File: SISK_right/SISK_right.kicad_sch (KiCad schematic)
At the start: 86 parts, among them J1 OLED_128x32, J2 Battery Conn, SW1 "6", SW10 "Z", SW11 "U", SW12 "I", SW13 "O", SW14 "P", SW15 "Ü", SW16 "*", SW17 "Enter", SW18 "Del", SW19 "H", SW2 "7", SW20 "J", SW21 "K", SW22 "L", SW23 "Ö", SW24 "Ä", SW25 "'", SW26 "PGUP", SW27 "N", SW28 "M", SW29 ";", SW3 "8", SW30 ":", SW31 "-", SW32 "shift_R", SW33 "UP", SW34 "PGDOWN", SW35 "SPACE_R", SW36 "Alt", SW37 FN, SW38 "Ctrl", SW39 "Left", SW4 "9", SW40 "Down", SW41 "Right", SW5 "0", SW6 "ß", SW7 "`", SW8 "Backspace", SW9 "^", U1 Nice_Nano_V2

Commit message: changed nice nano footprint
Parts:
- U1: footprint ScottoKeebs_MCU:Arduino_Pro_Micro -> nice-nano-kicad-master:nice_nano
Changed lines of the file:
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@@
 			)
 		)
-		(property "Footprint" "ScottoKeebs_MCU:Arduino_Pro_Micro"
+		(property "Footprint" "nice-nano-kicad-master:nice_nano"
 			(at 232.41 96.52 0)
 			(effects

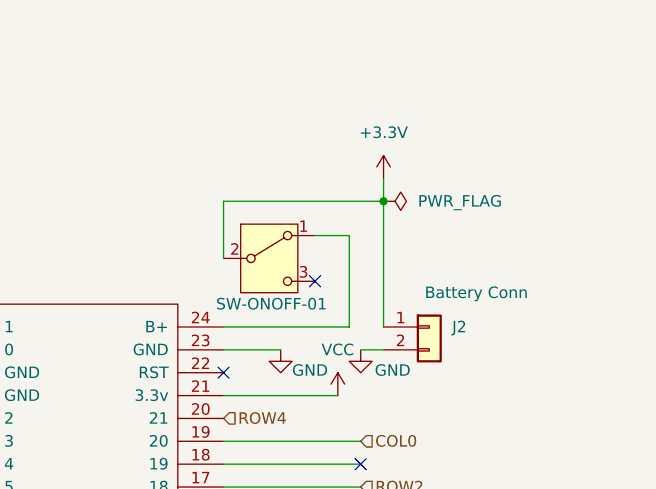
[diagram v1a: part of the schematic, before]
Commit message: added some text and alternative header for Power Switch
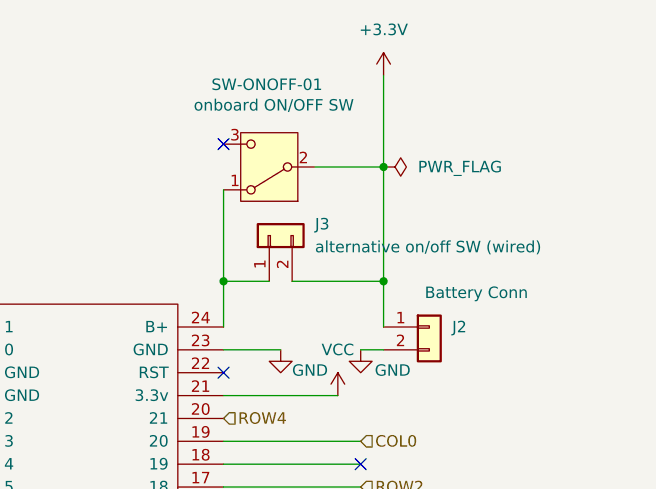
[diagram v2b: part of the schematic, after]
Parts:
- added J3: alternative on/off SW (wired), Connector_PinHeader_2.54mm:PinHeader_1x02_P2.54mm_Vertical, symbol Connector_Generic:Conn_01x02
- SW-ONOFF-01: value ~ -> onboard ON/OFF SW
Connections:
- net +3.3V: now also J3.2 (Pin_2)
- net at SW-ONOFF-01.1 (A), U1.24 (B+): now also J3.1 (Pin_1)
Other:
- moved on the sheet: SW-ONOFF-01
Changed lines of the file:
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@@
 	)
 	(junction
+		(at 265.43 41.91)
+		(diameter 0)
+		(color 0 0 0 0)
+	)
+	(junction
 		(at 74.93 85.09)
 		(diameter 0)
@@
 	)
 	(junction
+		(at 247.65 54.61)
+		(diameter 0)
+		(color 0 0 0 0)
+	)
+	(junction
 		(at 147.32 60.96)
 		(diameter 0)
@@
 	)
 	(junction
-		(at 265.43 45.72)
-		(diameter 0)
-		(color 0 0 0 0)
-	)
-	(junction
 		(at 116.84 60.96)
 		(diameter 0)
@@
 	)
 	(junction
+		(at 265.43 54.61)
+		(diameter 0)
+		(color 0 0 0 0)
+	)
+	(junction
 		(at 180.34 46.99)
 		(diameter 0)
@@
 	)
 	(no_connect
-		(at 257.81 54.61)
+		(at 247.65 39.37)
 	)
 	(no_connect
@@
 	(wire
 		(pts
-			(xy 261.62 49.53) (xy 257.81 49.53)
+			(xy 247.65 59.69) (xy 247.65 54.61)
 		)
 		(stroke
@@
 	(wire
 		(pts
-			(xy 247.65 52.07) (xy 247.65 45.72)
+			(xy 127 90.17) (xy 127 92.71)
 		)
 		(stroke
@@
 	(wire
 		(pts
-			(xy 127 90.17) (xy 127 92.71)
+			(xy 111.76 113.03) (xy 127 113.03)
 		)
 		(stroke
@@
 	(wire
 		(pts
-			(xy 111.76 113.03) (xy 127 113.03)
+			(xy 265.43 54.61) (xy 265.43 59.69)
 		)
 		(stroke
@@
 	(wire
 		(pts
-			(xy 261.62 59.69) (xy 261.62 49.53)
-		)
-		(stroke
-			(width 0)
-			(type default)
-		)
-	)
-	(wire
-		(pts
 			(xy 173.99 57.15) (xy 190.5 57.15)
 		)
@@
 	(wire
 		(pts
-			(xy 265.43 43.18) (xy 265.43 45.72)
-		)
-		(stroke
-			(width 0)
-			(type default)
-		)
-	)
-	(wire
-		(pts
 			(xy 217.17 67.31) (xy 210.82 67.31)
 		)
@@
 	(wire
 		(pts
-			(xy 247.65 59.69) (xy 261.62 59.69)
+			(xy 255.27 54.61) (xy 265.43 54.61)
+		)
+		(stroke
+			(width 0)
+			(type default)
+		)
+	)
+	(wire
+		(pts
+			(xy 247.65 54.61) (xy 247.65 44.45)
 		)
 		(stroke
@@
 	(wire
 		(pts
+			(xy 265.43 41.91) (xy 257.81 41.91)
+		)
+		(stroke
+			(width 0)
+			(type default)
+		)
+	)
+	(wire
+		(pts
 			(xy 127 85.09) (xy 142.24 85.09)
 		)
@@
 	(wire
 		(pts
+			(xy 265.43 31.75) (xy 265.43 41.91)
+		)
+		(stroke
+			(width 0)
+			(type default)
+		)
+	)
+	(wire
+		(pts
 			(xy 111.76 46.99) (xy 111.76 49.53)
 		)
@@
 	(wire
 		(pts
+			(xy 247.65 54.61) (xy 252.73 54.61)
+		)
+		(stroke
+			(width 0)
+			(type default)
+		)
+	)
+	(wire
+		(pts
 			(xy 83.82 90.17) (xy 83.82 104.14)
 		)
@@
 	(wire
 		(pts
-			(xy 265.43 45.72) (xy 265.43 59.69)
+			(xy 265.43 41.91) (xy 265.43 54.61)
 		)
 		(stroke
@@
 	(wire
 		(pts
-			(xy 247.65 45.72) (xy 265.43 45.72)
-		)
-		(stroke
-			(width 0)
-			(type default)
-		)
-	)
-	(wire
-		(pts
 			(xy 74.93 100.33) (xy 57.15 100.33)
 		)
@@
 	(symbol
 		(lib_id "power:PWR_FLAG")
-		(at 265.43 45.72 270)
+		(at 265.43 41.91 270)
 		(unit 1)
 		(exclude_from_sim no)
@@
 		(fields_autoplaced yes)
 		(property "Reference" "#FLG01"
-			(at 267.335 45.72 0)
+			(at 267.335 41.91 0)
 			(effects
 				(font
@@
 		)
 		(property "Value" "PWR_FLAG"
-			(at 269.24 45.7199 90)
+			(at 269.24 41.9099 90)
 			(effects
 				(font
@@
 		)
 		(property "Footprint" ""
-			(at 265.43 45.72 0)
+			(at 265.43 41.91 0)
 			(effects
 				(font
@@
 		)
 		(property "Datasheet" "~"
-			(at 265.43 45.72 0)
+			(at 265.43 41.91 0)
 			(effects
 				(font
@@
 		)
 		(property "Description" "Special symbol for telling ERC where power comes from"
-			(at 265.43 45.72 0)
+			(at 265.43 41.91 0)
 			(effects
 				(font
@@
 	)
 	(symbol
+		(lib_id "Connector_Generic:Conn_01x02")
+		(at 252.73 49.53 90)
+		(unit 1)
+		(exclude_from_sim no)
+		(in_bom yes)
+		(on_board yes)
+		(dnp no)
+		(fields_autoplaced yes)
+		(property "Reference" "J3"
+			(at 257.81 48.2599 90)
+			(effects
+				(font
+					(size 1.27 1.27)
+				)
+				(justify right)
+			)
+		)
+		(property "Value" "alternative on/off SW (wired)"
+			(at 257.81 50.7999 90)
+			(effects
+				(font
+					(size 1.27 1.27)
+				)
+				(justify right)
+			)
+		)
+		(property "Footprint" "Connector_PinHeader_2.54mm:PinHeader_1x02_P2.54mm_Vertical"
+			(at 252.73 49.53 0)
+			(effects
+				(font
+					(size 1.27 1.27)
+				)
+				(hide yes)
+			)
+		)
+		(property "Datasheet" "~"
+			(at 252.73 49.53 0)
+			(effects
+				(font
+					(size 1.27 1.27)
+				)
+				(hide yes)
+			)
+		)
+		(property "Description" "Generic connector, single row, 01x02, script generated (kicad-library-utils/schlib/autogen/connector/)"
+			(at 252.73 49.53 0)
+			(effects
+				(font
+					(size 1.27 1.27)
+				)
+				(hide yes)
+			)
+		)
+		(pin "2"
+		)
+		(pin "1"
+		)
+		(instances
+			(project ""
+				(path "/257e25c7-95c4-4199-9825-6959824a558c"
+					(reference "J3")
+					(unit 1)
+				)
+			)
+		)
+	)
+	(symbol
 		(lib_id "Device:D")
 		(at 173.99 52.07 90)
@@
 	(symbol
 		(lib_id "Switch:SW_SPDT")
-		(at 252.73 52.07 0)
+		(at 252.73 41.91 180)
 		(unit 1)
 		(exclude_from_sim no)
@@
 		(dnp no)
 		(property "Reference" "SW-ONOFF-01"
-			(at 252.984 57.15 0)
+			(at 252.476 32.766 0)
 			(effects
 				(font
@@
 			)
 		)
-		(property "Value" "~"
-			(at 252.73 46.99 0)
+		(property "Value" "onboard ON/OFF SW"
+			(at 253.238 35.052 0)
 			(effects
 				(font
@@
 		)
 		(property "Footprint" "ScottoKeebs_Components:Switch_MSK12C02"
-			(at 252.73 52.07 0)
+			(at 252.73 41.91 0)
 			(effects
 				(font
@@
 		)
 		(property "Datasheet" "~"
-			(at 252.73 59.69 0)
+			(at 252.73 34.29 0)
 			(effects
 				(font
@@
 		)
 		(property "Description" "Switch, single pole double throw"
-			(at 252.73 52.07 0)
+			(at 252.73 41.91 0)
 			(effects
 				(font
@@
 	(symbol
 		(lib_id "power:+3.3V")
-		(at 265.43 43.18 0)
+		(at 265.43 31.75 0)
 		(unit 1)
 		(exclude_from_sim no)
@@
 		(fields_autoplaced yes)
 		(property "Reference" "#PWR01"
-			(at 265.43 46.99 0)
+			(at 265.43 35.56 0)
 			(effects
 				(font
@@
 		)
 		(property "Value" "+3.3V"
-			(at 265.43 38.1 0)
+			(at 265.43 26.67 0)
 			(effects
 				(font
@@
 		)
 		(property "Footprint" ""
-			(at 265.43 43.18 0)
+			(at 265.43 31.75 0)
 			(effects
 				(font
@@
 		)
 		(property "Datasheet" ""
-			(at 265.43 43.18 0)
+			(at 265.43 31.75 0)
 			(effects
 				(font
@@
 		)
 		(property "Description" "Power symbol creates a global label with name \"+3.3V\""
-			(at 265.43 43.18 0)
+			(at 265.43 31.75 0)
 			(effects
 				(font
